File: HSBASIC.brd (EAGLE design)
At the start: 44 x 44 mm, 26 parts, among them IC1 ESP12-SMT, IC2 BME280, J1 ESPROG-SOCKET, J2 I2C

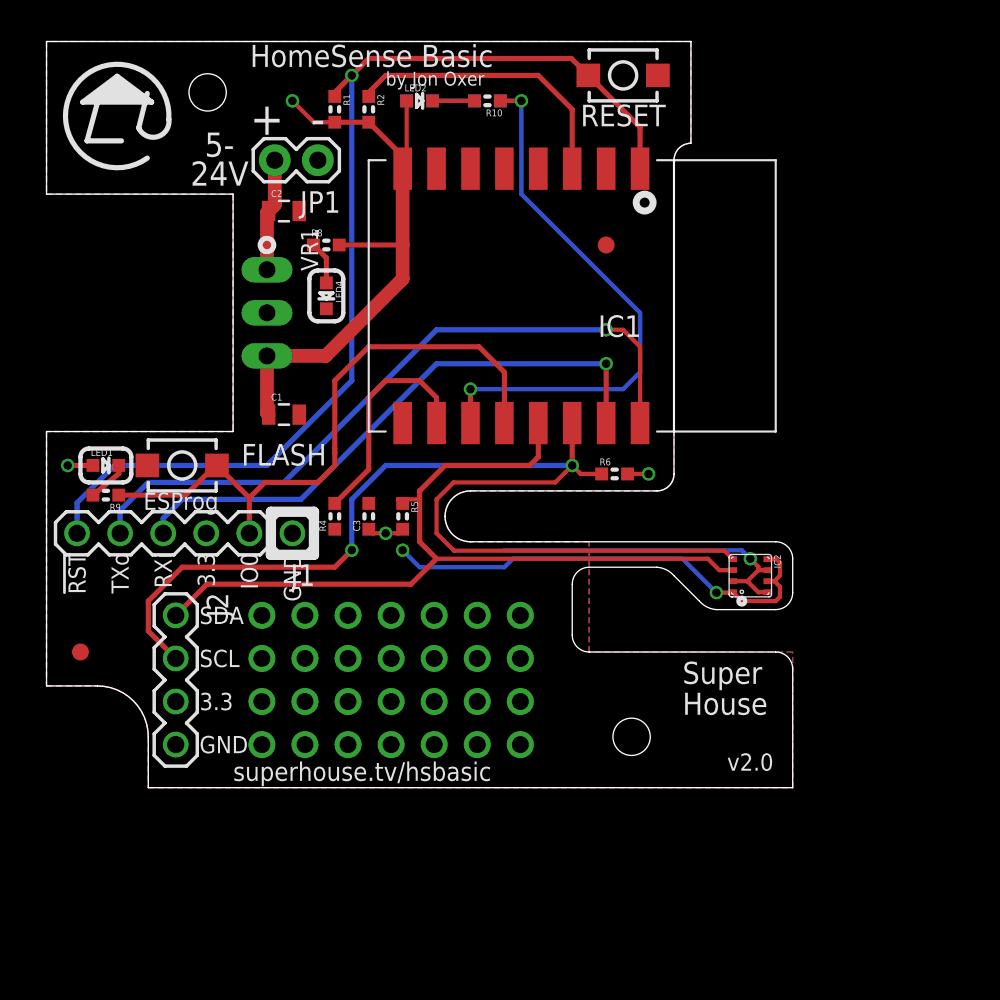
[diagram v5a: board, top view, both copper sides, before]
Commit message: Major restructure to add OLED and prototyping area
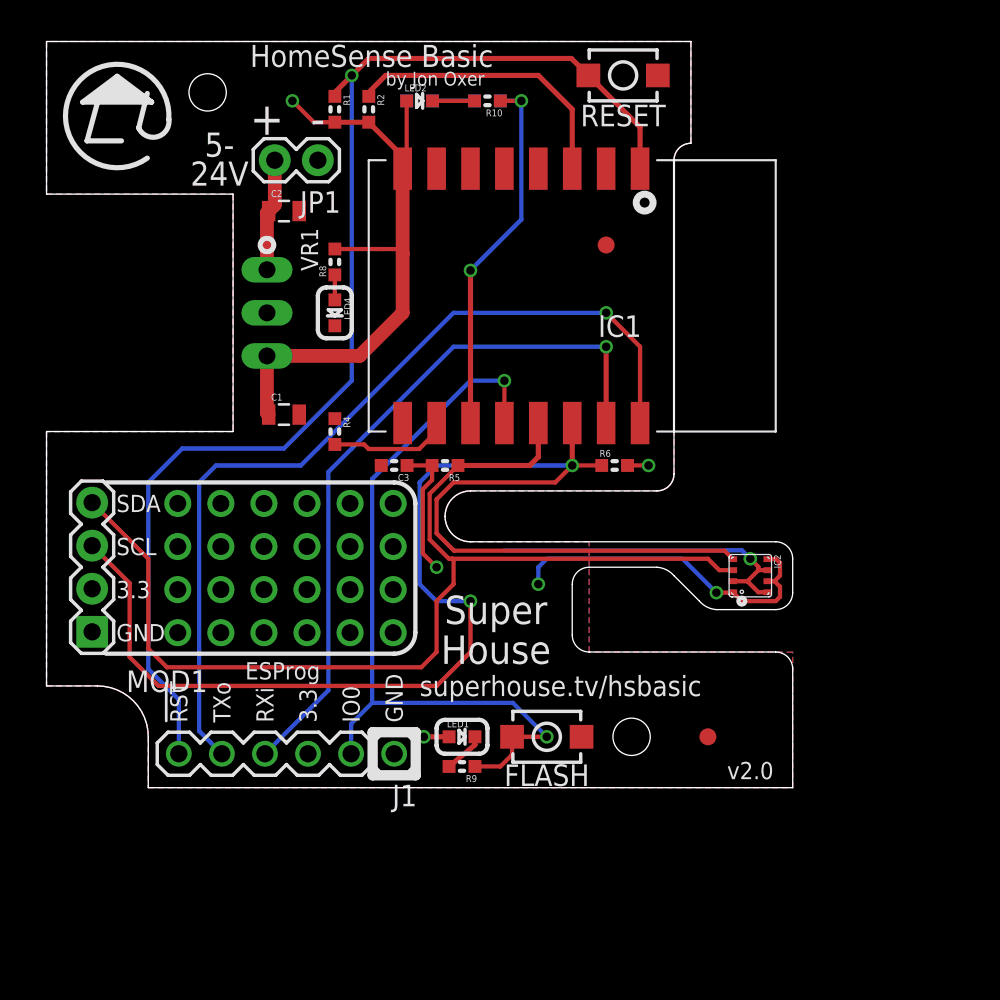
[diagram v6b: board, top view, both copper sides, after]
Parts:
- removed J2: I2C, SuperHouse-Connectors:1X04
- added MOD1: OLED-I2C128X32-0.91, SuperHouse-Displays:OLED-128X32-0.91
- moved FID2 37.3 mm to (39.0, 3.00)
- moved S2 26.8 mm to (29.5, 3.00), turned to 180 degrees
- moved LED1 26.4 mm to (24.5, 3.00)
- moved R9 26.4 mm to (24.5, 1.25)
- moved J1 14.3 mm to (20.5, 2.00)
- moved R4 5.00 mm to (17.0, 21.0), turned to 270 degrees
- moved R5 3.91 mm to (23.5, 19.0), turned to 180 degrees
- moved C3 3.35 mm to (20.5, 19.0), turned to 180 degrees
- moved LED4 1.12 mm to (17.0, 28.0)
- moved R8 1.12 mm to (17.0, 31.0), turned to 90 degrees
- moved R6 0.50 mm to (33.5, 19.0)
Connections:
- net 3.3V: now also MOD1.VCC; no longer J2.3
- net GND: now also MOD1.GND; no longer J2.4
- net SCL: now also MOD1.SCL; no longer J2.2
- net SDA: now also MOD1.SDA; no longer J2.1
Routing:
- net SCL: track 67.5 -> 84.1 mm
- net SDA: track 50.4 -> 64.4 mm
- net GPIO2: track 33.8 -> 22.7 mm
- net TXD: track 41.3 -> 52.0 mm
- net !RESET: track 62.2 -> 72.4 mm
- net GPIO0: track 36.6 -> 46.1 mm, vias 0 -> 2
- net RXD: track 34.3 -> 42.1 mm
- net GND: track 27.5 -> 20.1 mm
- net 3.3V: track 60.6 -> 68.0 mm
- net GPIO15: track 13.4 -> 7.04 mm
- net N$2: track 2.55 -> 1.48 mm
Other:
- board text added: "Copyright 2017-19 SuperHouse Automation Pty Ltd"
- board text removed: "Copyright 2017 SuperHouse Automation Pty Ltd"

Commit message: Final tweaks plus ERC and DRC for v2.0 release
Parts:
- FID2, FID3: device freetronics:FIDUCIAL-1X2.5 -> SuperHouse-Symbols:FIDUCIAL-1X2.5
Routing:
- net 3.3V: track 68.0 -> 72.4 mm
- net SCL: track 84.1 -> 83.4 mm
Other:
- board text added: "BME280: 0x76 SSD1306: 0x3C"
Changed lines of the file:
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@@
 <setting verticaltext="up"/>
 </settings>
-<grid distance="1" unitdist="mm" unit="mm" style="lines" multiple="1" display="yes" altdistance="5" altunitdist="mil" altunit="mil"/>
+<grid distance="39.3700787" unitdist="mil" unit="mil" style="lines" multiple="1" display="yes" altdistance="5" altunitdist="mil" altunit="mil"/>
 <layers>
 <layer number="1" name="Top" color="4" fill="1" visible="yes" active="yes"/>
@@
 </layers>
 <board>
-<fusionsync huburn="a.cGVyc29uYWw6dWUyZDliZmNi" projecturn="a.cGVyc29uYWw6dWUyZDliZmNiIzIwMTkwNjE5MTk5NjgzNjgx" f3durn="urn:adsk.wipprod:dm.lineage:OGjb5C-sRfSX_GoFxLdnUw" pcbguid="54a2e106-a76a-4605-8f7a-9ec732ccbce4" lastpulledtime="" lastsyncedchangeguid="c9fec659-94ba-a1b6-98c2-effe73a6487c"/>
+<fusionsync huburn="a.cGVyc29uYWw6dWUyZDliZmNi" projecturn="a.cGVyc29uYWw6dWUyZDliZmNiIzIwMTkwNjE5MTk5NjgzNjgx" f3durn="urn:adsk.wipprod:dm.lineage:OGjb5C-sRfSX_GoFxLdnUw" pcbguid="54a2e106-a76a-4605-8f7a-9ec732ccbce4" lastpulledtime="" lastsyncedchangeguid="630af7cb-d619-fa34-c694-e377fe52466c"/>
 <plain>
 <wire x1="0" y1="6" x2="0" y2="21" width="0.0254" layer="20"/>
@@
 <text x="16" y="38" size="1.6764" layer="22" font="vector" ratio="16" rot="MR0" align="bottom-center">-</text>
 <text x="6.5" y="36" size="1.6764" layer="22" font="vector" ratio="16" rot="MR0" align="bottom-center">5-24Vdc</text>
-<text x="26.5" y="7.3" size="1.6764" layer="21" font="vector" ratio="18" distance="40" align="bottom-center">Super
+<text x="26.5" y="7.3" size="1.6764" layer="21" font="vector" ratio="18" distance="20" align="bottom-center">Super
 House</text>
 <wire x1="26" y1="3.5" x2="25.5" y2="4" width="0.254" layer="21" curve="90"/>
@@
 <text x="14.5" y="30.5" size="1.4224" layer="22" font="vector" ratio="16" rot="MR0" align="center-right">IN</text>
 <text x="14.5" y="25.5" size="1.4224" layer="22" font="vector" ratio="16" rot="MR0" align="center-right">OUT</text>
-<text x="4.117" y="16.76" size="1.016" layer="21" font="vector" ratio="16" align="center-left">SDA</text>
-<text x="4.117" y="14.22" size="1.016" layer="21" font="vector" ratio="16" align="center-left">SCL</text>
-<text x="4.117" y="11.68" size="1.016" layer="21" font="vector" ratio="16" align="center-left">3.3</text>
-<text x="4.117" y="9.14" size="1.016" layer="21" font="vector" ratio="16" align="center-left">GND</text>
+<text x="2.417" y="16.76" size="0.8128" layer="21" font="vector" ratio="16" align="center-right">SDA</text>
+<text x="2.417" y="14.22" size="0.8128" layer="21" font="vector" ratio="16" align="center-right">SCL</text>
+<text x="2.417" y="11.68" size="0.8128" layer="21" font="vector" ratio="16" align="center-right">3.3</text>
+<text x="2.417" y="9.14" size="0.8128" layer="21" font="vector" ratio="16" align="center-right">GND</text>
 <text x="20.5" y="3.843" size="1.016" layer="21" font="vector" ratio="16" rot="R270" align="center-right">GND</text>
 <text x="15.42" y="3.843" size="1.016" layer="21" font="vector" ratio="16" rot="R270" align="center-right">3.3</text>
@@
 <text x="10.2" y="35.5" size="1.4224" layer="21" font="vector" ratio="16" distance="20" align="bottom-center">5-
 24V</text>
-<wire x1="3.5" y1="18" x2="20.5" y2="18" width="0.254" layer="21"/>
+<wire x1="4.5" y1="18" x2="20.5" y2="18" width="0.254" layer="21"/>
 <wire x1="20.5" y1="18" x2="21.75" y2="16.75" width="0.254" layer="21" curve="-90"/>
 <wire x1="21.75" y1="16.75" x2="21.75" y2="9.15" width="0.254" layer="21"/>
-<wire x1="3.5" y1="7.9" x2="20.5" y2="7.9" width="0.254" layer="21"/>
+<wire x1="4.5" y1="7.9" x2="20.5" y2="7.9" width="0.254" layer="21"/>
 <wire x1="20.5" y1="7.9" x2="21.75" y2="9.15" width="0.254" layer="21" curve="90"/>
+<text x="0.5" y="18.5" size="1.016" layer="21" font="vector" ratio="16" distance="20">BME280: 0x76
+SSD1306: 0x3C</text>
 </plain>
 <attributes>
@@
 </class>
 </classes>
-<designrules name="ElectroDragon_2layer_DRU_no_angle_20140221">
+<designrules name="ElectroDragon_2layer_DRU_no_angle_20140221 *">
 <description language="de">&lt;b&gt;EAGLE Design Rules&lt;/b&gt;
 &lt;p&gt;
@@
 <param name="mlMinCreamFrame" value="0mil"/>
 <param name="mlMaxCreamFrame" value="0mil"/>
-<param name="mlViaStopLimit" value="100mil"/>
+<param name="mlViaStopLimit" value="25mil"/>
 <param name="srRoundness" value="0"/>
 <param name="srMinRoundness" value="0mil"/>
@@
 <attribute name="VALUE" x="21.77" y="5.175" size="1.27" layer="27" rot="R180"/>
 </element>
-<element name="FID2" library="freetronics" package="FIDUCIAL-1X2.5" value="FIDUCIAL1X2.5" x="39" y="3" smashed="yes"/>
-<element name="FID3" library="freetronics" package="FIDUCIAL-1X2.5" value="FIDUCIAL1X2.5" x="33" y="32" smashed="yes"/>
-<element name="MOD1" library="SuperHouse-Displays" library_urn="urn:adsk.eagle:library:11966779" package="OLED-128X32-0.91" package3d_urn="urn:adsk.eagle:package:11973684/2" value="OLED-I2C128X32-0.91" x="22" y="13" locked="yes" smashed="yes">
+<element name="FID2" library="SuperHouse-Symbols" library_urn="urn:adsk.eagle:library:13228893" package="FIDUCIAL-1X2.5" package3d_urn="urn:adsk.eagle:package:13228898/1" value="FIDUCIAL1X2.5" x="39" y="3" smashed="yes"/>
+<element name="FID3" library="SuperHouse-Symbols" library_urn="urn:adsk.eagle:library:13228893" package="FIDUCIAL-1X2.5" package3d_urn="urn:adsk.eagle:package:13228898/1" value="FIDUCIAL1X2.5" x="33" y="32" smashed="yes"/>
+<element name="MOD1" library="SuperHouse-Displays" library_urn="urn:adsk.eagle:library:11966779" package="OLED-128X32-0.91" package3d_urn="urn:adsk.eagle:package:11973684/4" value="OLED-I2C128X32-0.91" x="22" y="13" locked="yes" smashed="yes">
 <attribute name="NAME" x="4.7038" y="5.6388" locked="yes" size="1.27" layer="25" ratio="10"/>
 <attribute name="VALUE" x="4.78" y="19.675" locked="yes" size="1.27" layer="27"/>
@@
 <wire x1="22.5936" y1="14.6316625" x2="22.5936" y2="17.3316" width="0.254" layer="1"/>
 <contactref element="MOD1" pad="SDA"/>
-<wire x1="2.69" y1="16.81" x2="6" y2="13.5" width="0.254" layer="1"/>
-<wire x1="6" y1="13.5" x2="6" y2="8.2" width="0.254" layer="1"/>
+<wire x1="6" y1="8.2" x2="6" y2="13.5" width="0.254" layer="1"/>
 <wire x1="6" y1="8.2" x2="7.1" y2="7.1" width="0.254" layer="1"/>
 <wire x1="22.1" y1="7.1" x2="23" y2="8" width="0.254" layer="1"/>
@@
 <wire x1="24" y1="12" x2="24" y2="13.4252625" width="0.254" layer="1"/>
 <wire x1="24" y1="13.4252625" x2="23.9252625" y2="13.5" width="0.254" layer="1"/>
+<wire x1="6" y1="13.5" x2="6" y2="14.5" width="0.254" layer="1"/>
+<wire x1="6" y1="14.5" x2="3.69" y2="16.81" width="0.254" layer="1"/>
 </signal>
 <signal name="SCL">
@@
 <wire x1="32.738" y1="19" x2="31" y2="19" width="0.254" layer="1"/>
 <contactref element="MOD1" pad="SCL"/>
-<wire x1="2.69" y1="14.27" x2="4.9" y2="12.06" width="0.254" layer="1"/>
-<wire x1="4.9" y1="12.06" x2="4.9" y2="7.7" width="0.254" layer="1"/>
-<wire x1="4.9" y1="7.7" x2="6.6" y2="6" width="0.254" layer="1"/>
+<wire x1="5.4" y1="7.7" x2="5.4" y2="12.06" width="0.254" layer="1"/>
+<wire x1="5.4" y1="7.7" x2="7.1" y2="6" width="0.254" layer="1"/>
 <wire x1="25" y1="8" x2="25" y2="11" width="0.254" layer="1"/>
-<wire x1="6.6" y1="6" x2="23" y2="6" width="0.254" layer="1"/>
+<wire x1="7.1" y1="6" x2="23" y2="6" width="0.254" layer="1"/>
 <wire x1="23" y1="6" x2="25" y2="8" width="0.254" layer="1"/>
 <via x="25" y="11" extent="1-16" drill="0.5"/>
@@
 <wire x1="22" y1="18" x2="23" y2="19" width="0.254" layer="16"/>
 <wire x1="23" y1="19" x2="31" y2="19" width="0.254" layer="16"/>
+<wire x1="5.4" y1="12.06" x2="5.4" y2="12.56" width="0.254" layer="1"/>
+<wire x1="5.4" y1="12.56" x2="3.69" y2="14.27" width="0.254" layer="1"/>
 </signal>
 <signal name="GPIO0">
@@
 <wire x1="34.262" y1="19" x2="35.5" y2="19" width="0.254" layer="1"/>
 <wire x1="41.5" y1="13.5" x2="41" y2="14" width="0.254" layer="16"/>
-<wire x1="41" y1="14" x2="27" y2="14" width="0.254" layer="16"/>
 <via x="22.25" y="3" extent="1-16" drill="0.5"/>
 <wire x1="23.738" y1="3" x2="22.25" y2="3" width="0.3048" layer="1"/>
@@
 <wire x1="22.1872" y1="17.5999375" x2="22.1872" y2="13.8128" width="0.254" layer="1"/>
 <wire x1="22.1872" y1="13.8128" x2="23" y2="13" width="0.254" layer="1"/>
-<wire x1="17" y1="31.762" x2="19.5" y2="31.762" width="0.254" layer="1"/>
-<wire x1="19.5" y1="31.762" x2="19.762" y2="31.762" width="0.254" layer="1"/>
-<wire x1="19.762" y1="31.762" x2="20.738" y2="31.762" width="0.254" layer="1"/>
+<wire x1="17" y1="31.762" x2="20.738" y2="31.762" width="0.254" layer="1"/>
 <wire x1="20.738" y1="31.762" x2="21" y2="31.5" width="0.254" layer="1"/>
+<wire x1="24" y1="14" x2="23" y2="13" width="0.254" layer="16"/>
+<wire x1="41" y1="14" x2="24" y2="14" width="0.254" layer="16"/>
 </signal>
 <signal name="N$3">
